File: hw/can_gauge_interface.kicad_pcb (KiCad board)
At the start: 2 copper layers, 58 parts, among them J1 USB_B, J10 Conn_01x01_Socket, J2 Conn_02x04_Top_Bottom, J3 Analog, J4 ICSP, J5 SPI debug, J6 Conn_01x01_Socket, J7 Conn_01x01_Socket, J8 Conn_01x01_Socket, J9 Conn_01x01_Socket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

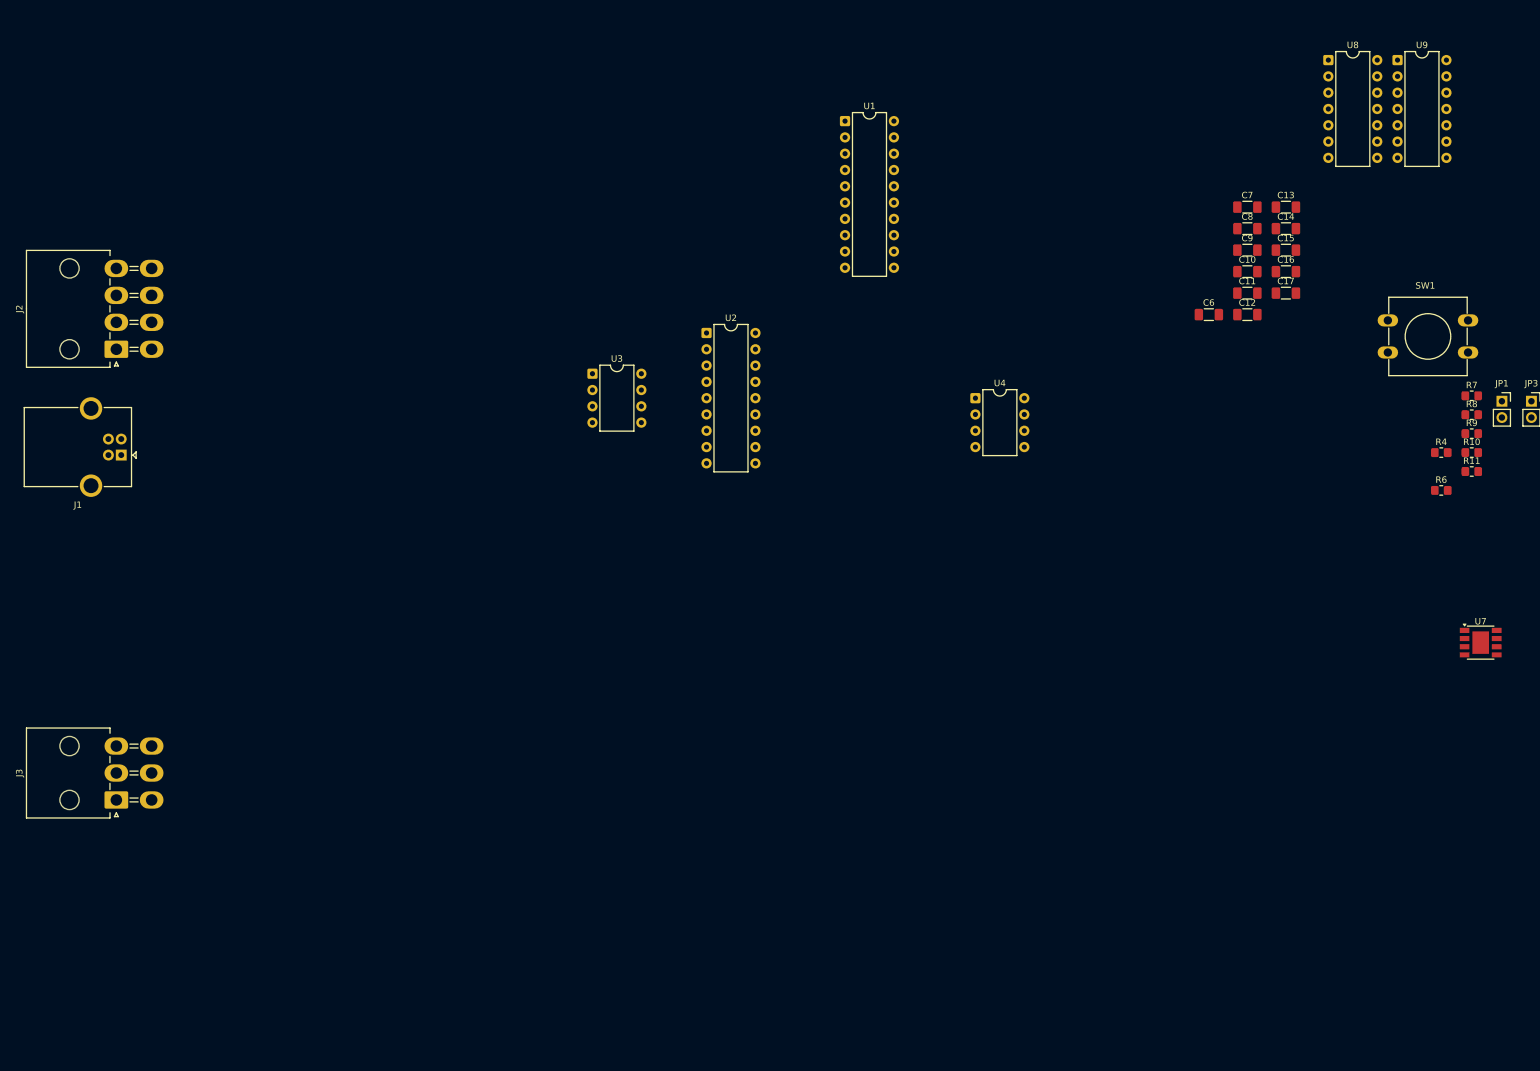
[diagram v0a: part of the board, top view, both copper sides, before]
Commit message: analog ldo layout and routing
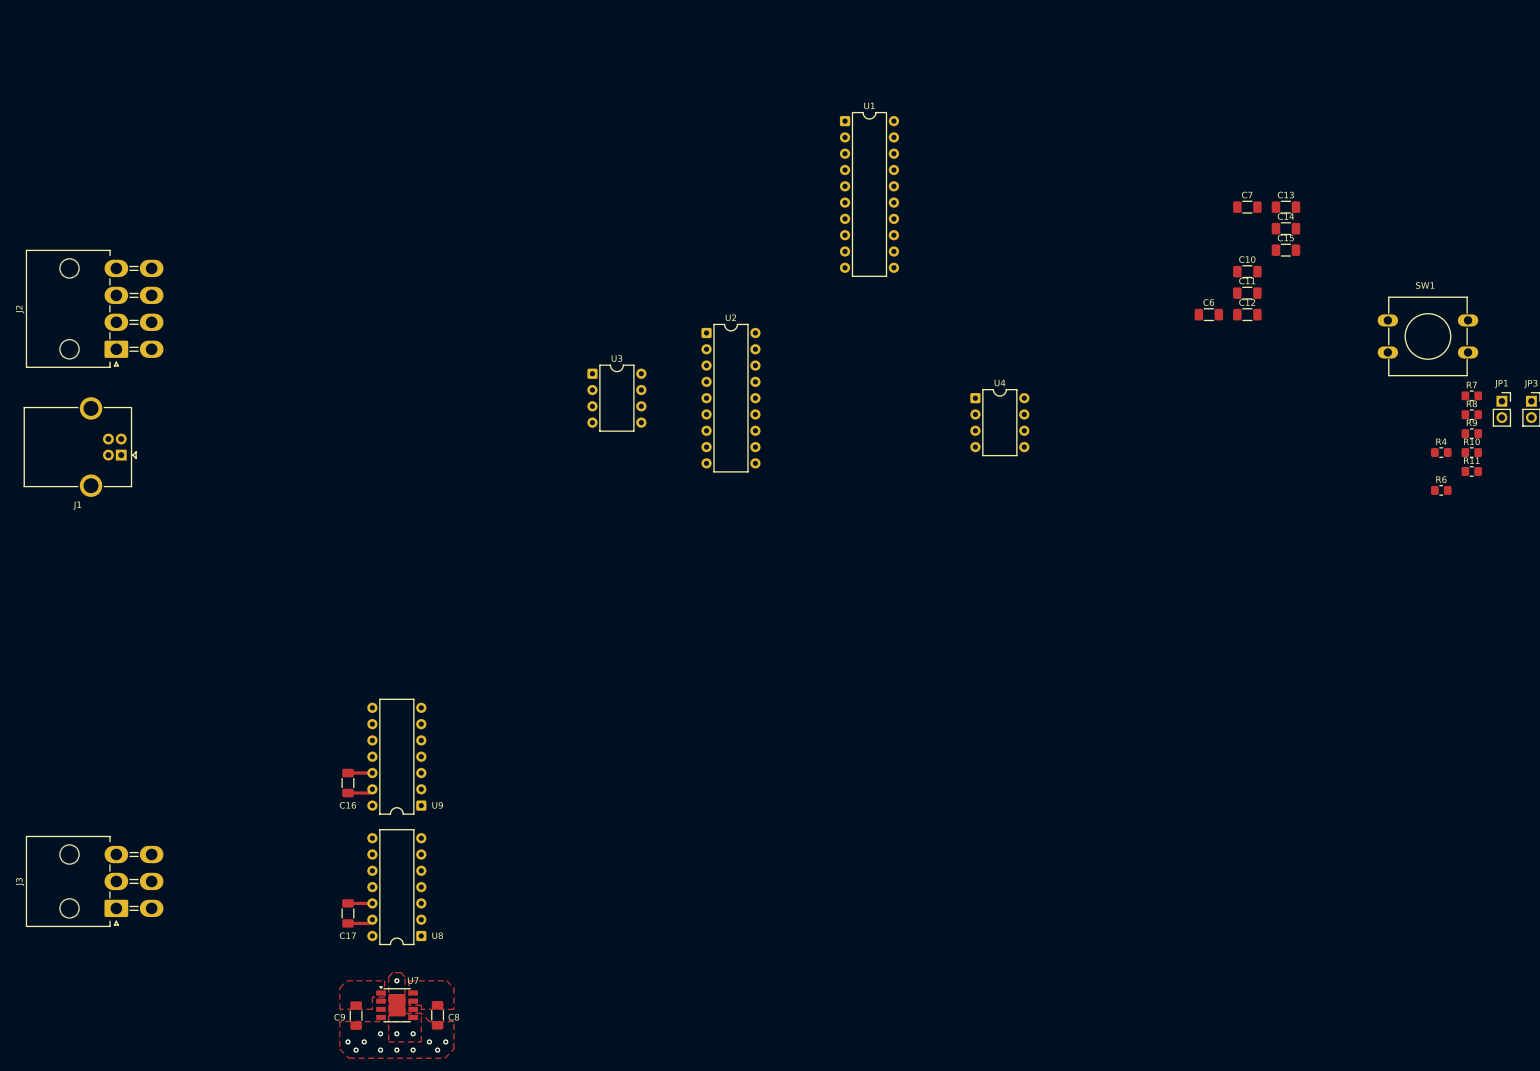
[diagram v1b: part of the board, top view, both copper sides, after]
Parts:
- moved U8 196.5 mm to (86.4, 218.4), turned to 180 degrees
- moved U9 191.4 mm to (86.4, 198.1), turned to 180 degrees
- moved C9 183.1 mm to (76.2, 230.8), turned to -90 degrees
- moved U7 178.1 mm to (82.6, 229.2)
- moved C8 175.9 mm to (88.9, 230.8), turned to -90 degrees
- moved C17 175.3 mm to (74.9, 214.9), turned to 90 degrees
- moved C16 166.5 mm to (74.9, 194.6), turned to 90 degrees
- moved J3 16.9 mm to (38.8, 214.1)
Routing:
- net +5VA: track 0.00 -> 8.10 mm
- net GND: track 10.2 -> 17.8 mm, vias 24 -> 37
- added copper zone on F.Cu, net +5VA

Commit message: analog routing
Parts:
- moved C9 46.2 mm to (116.5, 208.4), turned to 0 degrees
- moved C8 44.6 mm to (116.5, 195.7), turned to 0 degrees
- moved U7 42.3 mm to (114.9, 202.0), turned to 90 degrees
- moved C17 30.3 mm to (102.9, 203.2), turned to -90 degrees
- moved U8 23.3 mm to (97.8, 198.1), turned to -90 degrees
- moved U9 15.2 mm to (71.1, 198.1), turned to -90 degrees
- moved C16 8.69 mm to (76.2, 203.2), turned to -90 degrees
- moved J3 3.69 mm to (40.2, 217.6)
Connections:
- J3 pad 3: /AN3 -> /AN4
- J3 pad 6: /AN4 -> /AN3
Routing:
- net +5VA: track 8.10 -> 95.2 mm
- net /AN1: track 0.00 -> 67.8 mm
- net /AN2: track 0.00 -> 47.5 mm
- net /AN3: track 0.00 -> 32.2 mm
- net /AN4: track 0.00 -> 26.0 mm
- net GND: track 17.8 -> 10.2 mm, vias 37 -> 41

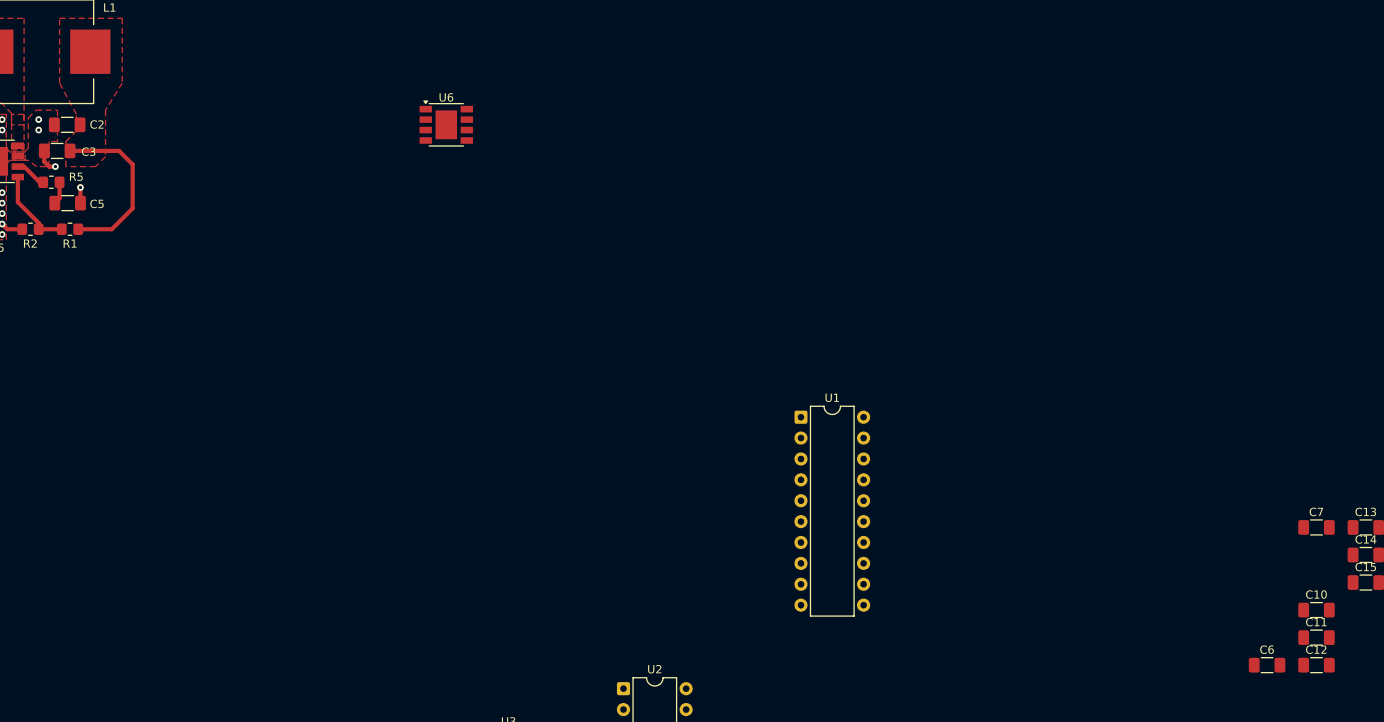
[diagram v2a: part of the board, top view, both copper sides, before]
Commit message: digital ldo layout and routing
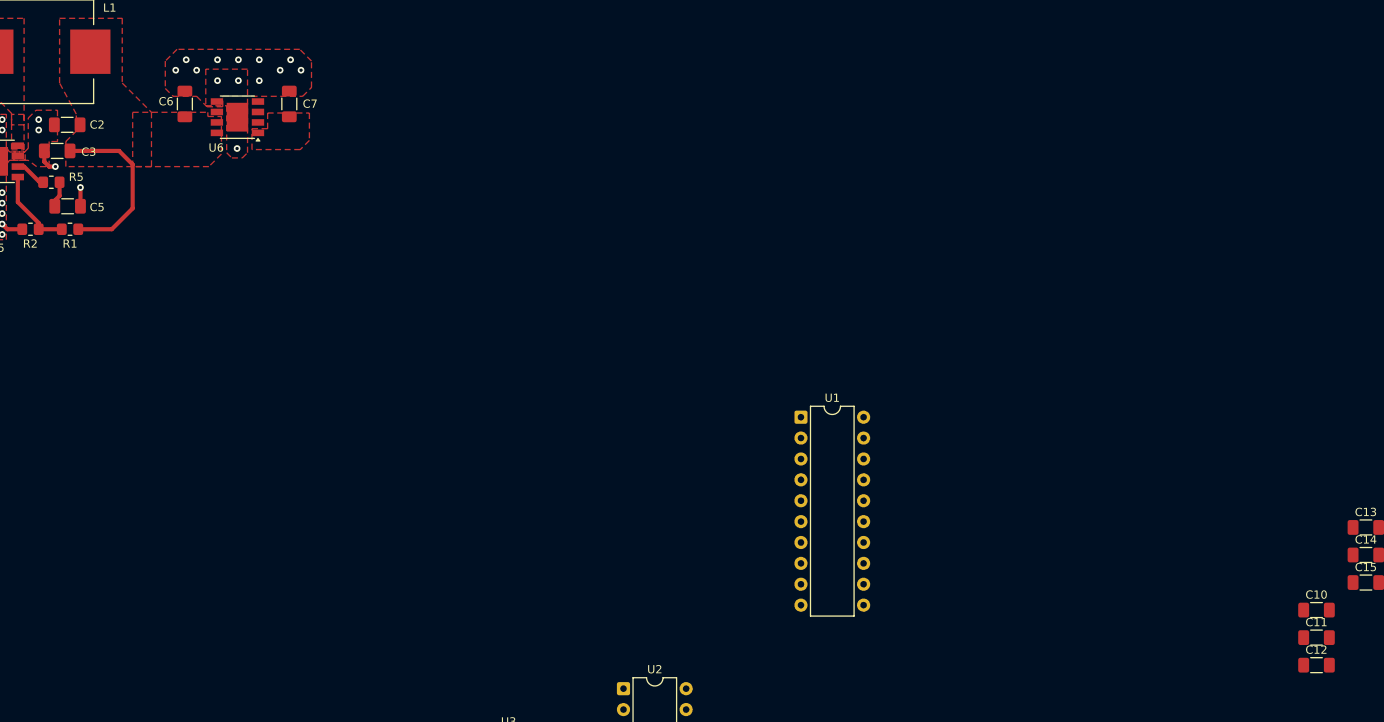
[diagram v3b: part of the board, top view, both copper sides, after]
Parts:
- moved C6 148.3 mm to (77.5, 53.3), turned to 90 degrees
- moved C7 135.1 mm to (90.2, 53.3), turned to 90 degrees
- moved U6 25.4 mm to (83.9, 55.0), turned to 180 degrees
- moved C5 0.38 mm to (63.2, 65.8)
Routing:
- net GND: track 10.2 -> 10.6 mm, vias 41 -> 54
- added copper zone on F.Cu, net +5V

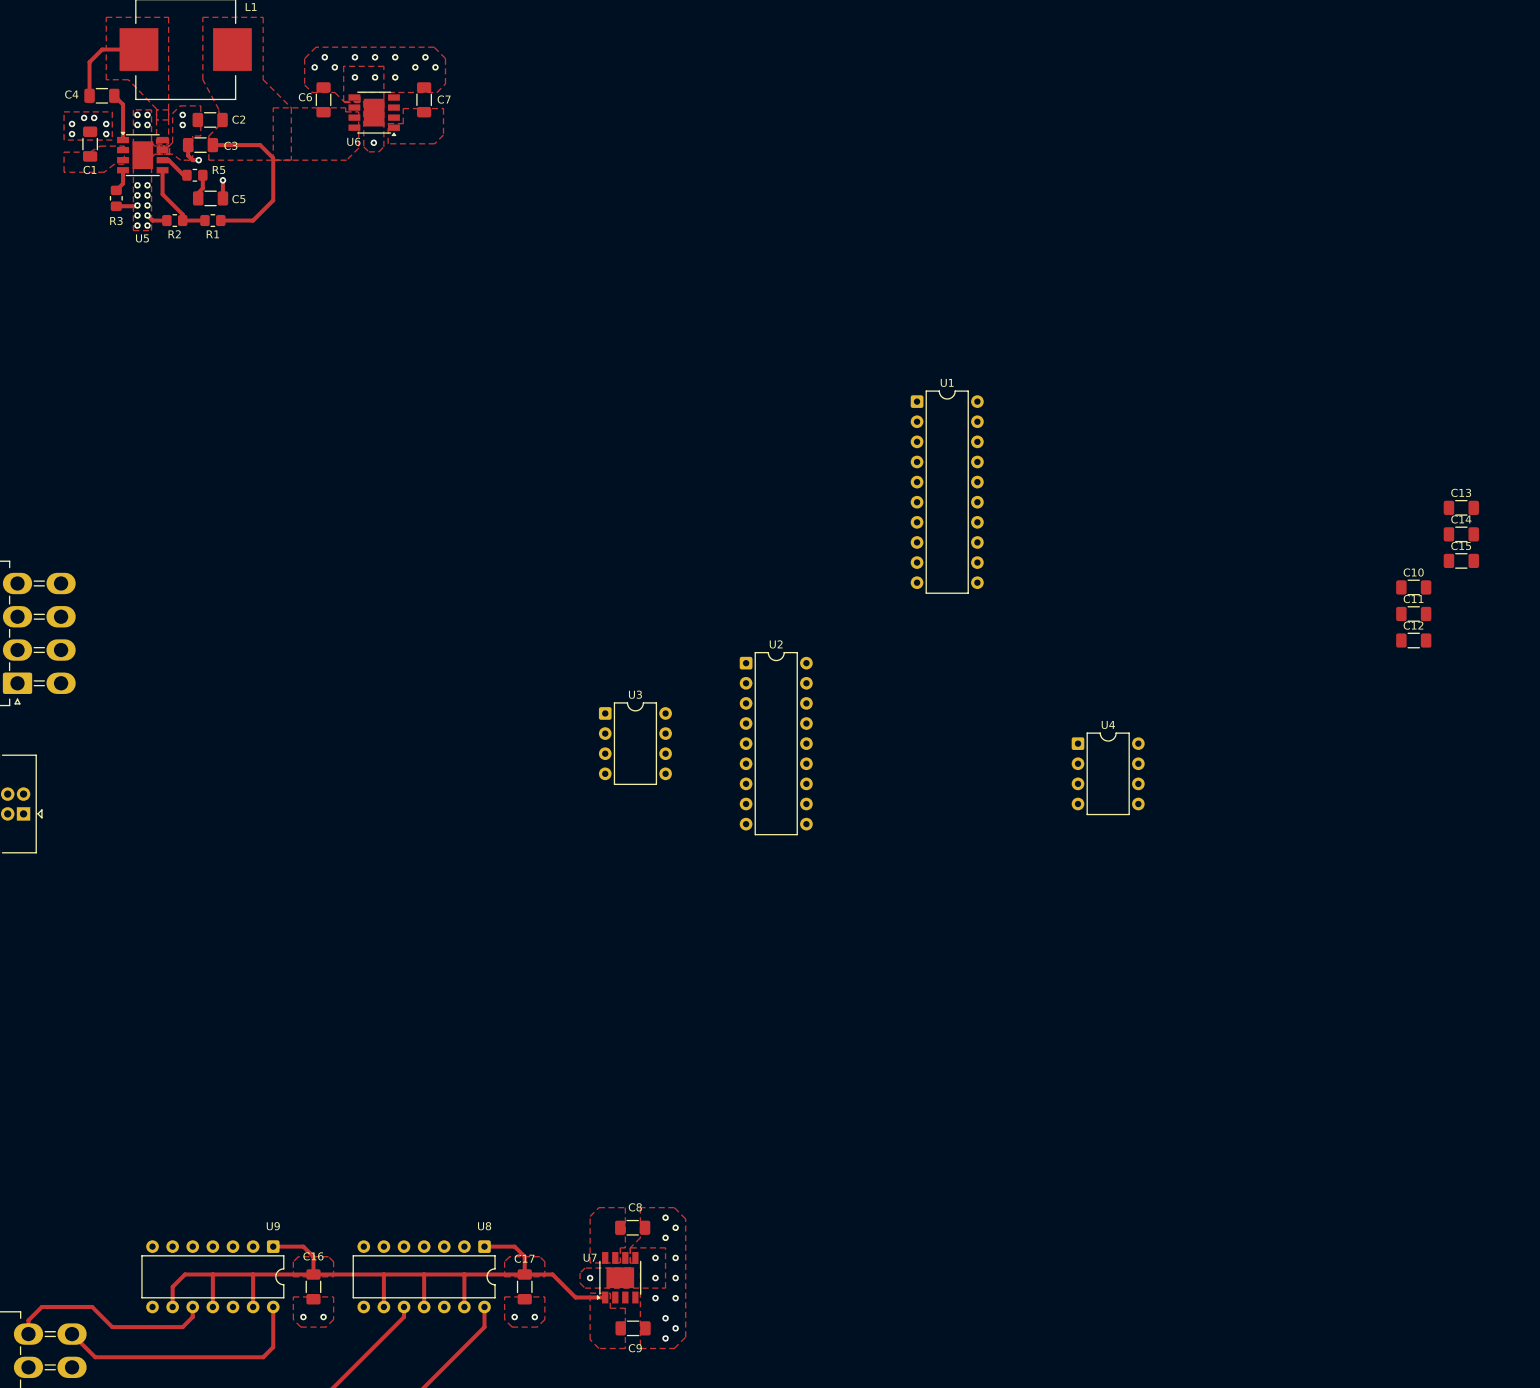
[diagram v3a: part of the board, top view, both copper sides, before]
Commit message: tht decoupling caps
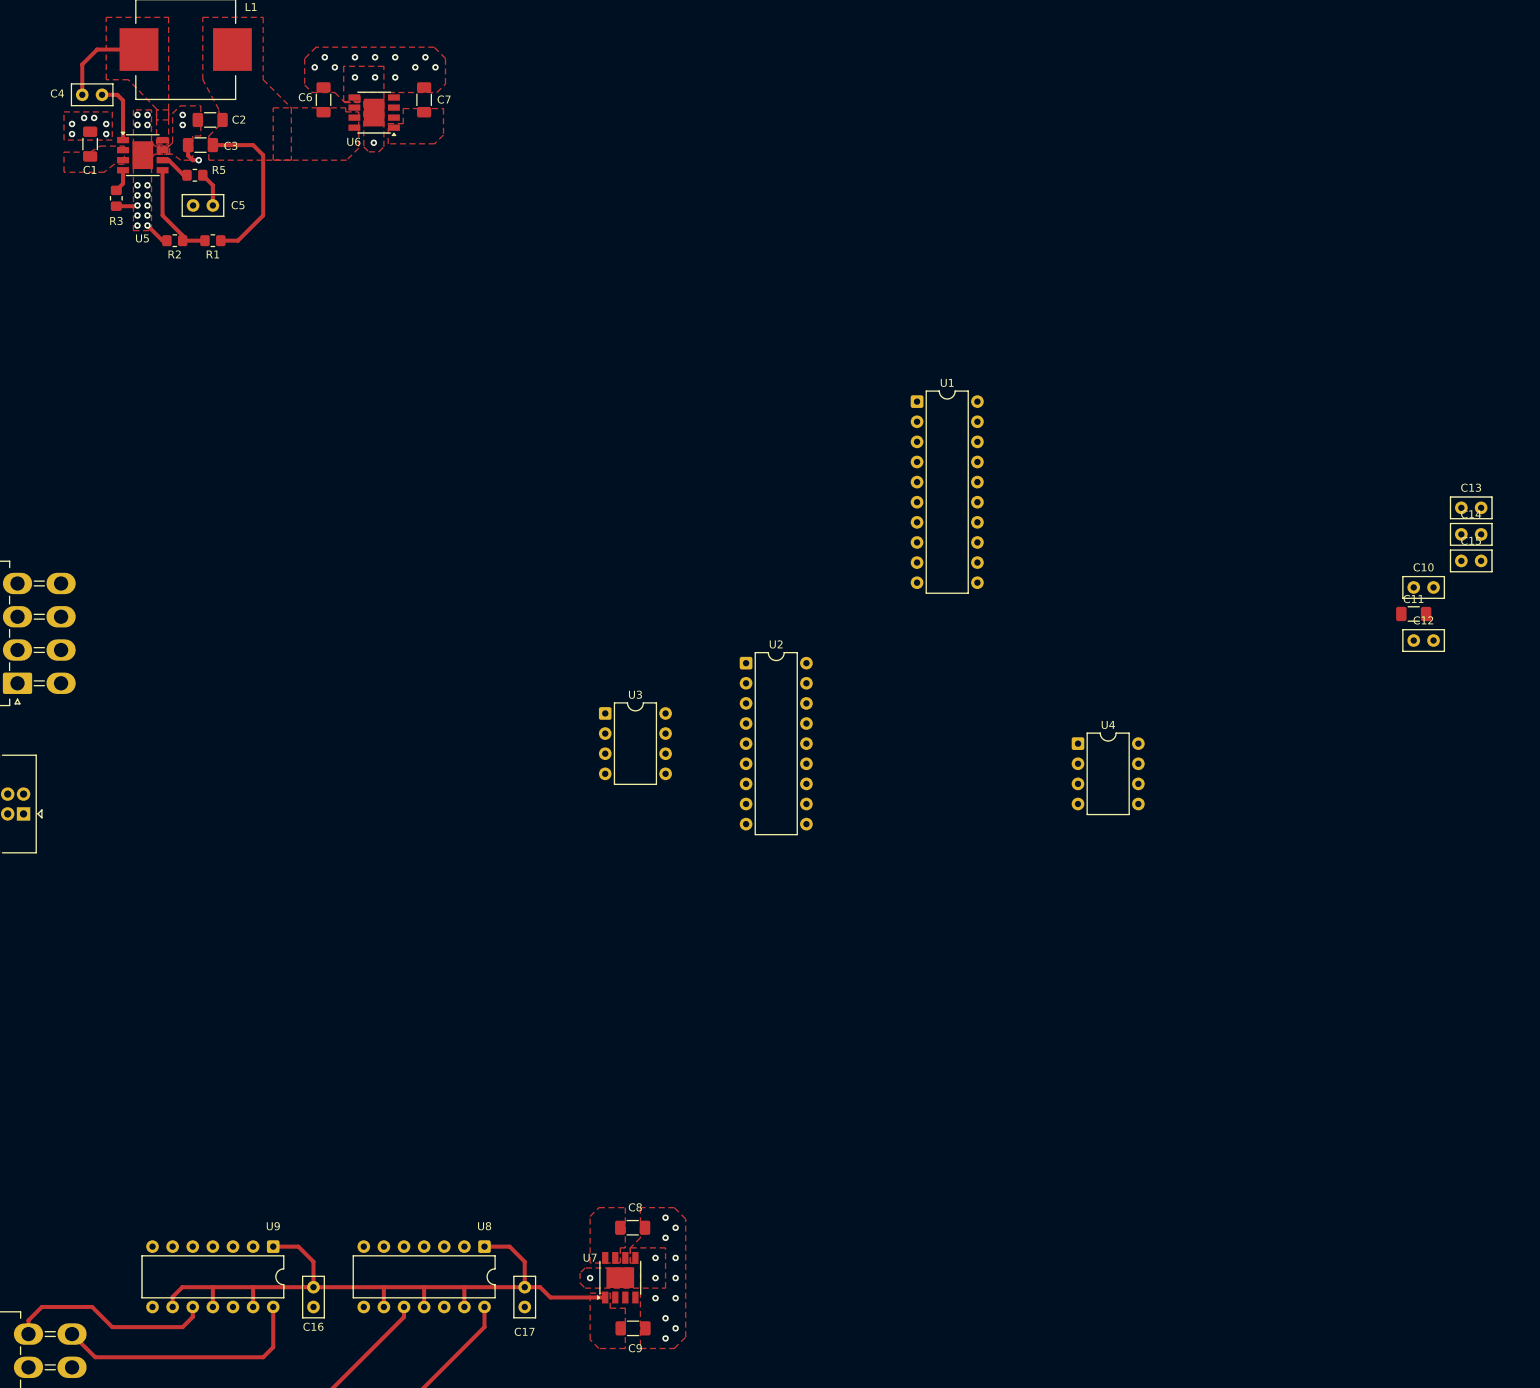
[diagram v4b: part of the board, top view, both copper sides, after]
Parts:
- C10, C12, C13, C14, C15, C16, C17, C4, C5: footprint Capacitor_SMD:C_1206_3216Metric_Pad1.33x1.80mm_HandSolder -> Capacitor_THT:C_Disc_D5.0mm_W2.5mm_P2.50mm
- moved R1 2.54 mm to (63.5, 71.1)
- moved R2 2.54 mm to (58.7, 71.1)
- moved C4 2.48 mm to (47.0, 52.7)
- moved C5 2.38 mm to (61.0, 66.7), turned to 0 degrees
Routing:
- net +5VA: track 95.2 -> 87.6 mm
- net Net-(U5-FB): track 10.2 -> 12.8 mm
- net Net-(U5-BST): track 6.04 -> 7.94 mm
- net GND: track 10.6 -> 8.85 mm, vias 54 -> 49
- net Net-(C5-Pad2): track 3.16 -> 4.34 mm
- net Net-(U5-SW): track 11.1 -> 11.8 mm
